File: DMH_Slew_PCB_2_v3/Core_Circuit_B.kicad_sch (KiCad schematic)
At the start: 48 parts, among them J6 TS_Jack_6.35mm_Sw, J60 Conn_01x08_PinHeader, J61 Conn_01x08_PinHeader, J7 TS_Jack_6.35mm_Sw, J8 TS_Jack_6.35mm_Sw, Q10 BC558, Q7 BC548, Q8 BC548, Q9 BC558, SW4 SW_DPDT_3way, SW5 SW_DPDT, SW6 SPDT_OnOffOn, U3 TL074, U4 TL074

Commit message: Relinked PCB1 and 2 with new v3 schematics
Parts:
- removed J60, J61: Conn_01x08_PinHeader, Connector_PinSocket_2.54mm:PinSocket_1x08_P2.54mm_Vertical, symbol SynthStuff:Conn_01x08_PinHeader
- removed R69, R70: 1k, Resistor_THT:R_Axial_DIN0207_L6.3mm_D2.5mm_P7.62mm_Horizontal, symbol Device:R_US
- removed R71, R72: 100k, Resistor_THT:R_Axial_DIN0207_L6.3mm_D2.5mm_P7.62mm_Horizontal, symbol Device:R_US
- removed R73: 220k, Resistor_THT:R_Axial_DIN0207_L6.3mm_D2.5mm_P7.62mm_Horizontal, symbol Device:R_US
- removed R74: 10k, Resistor_THT:R_Axial_DIN0207_L6.3mm_D2.5mm_P7.62mm_Horizontal, symbol Device:R_US
- removed R75, R76: 1k8, Resistor_THT:R_Axial_DIN0207_L6.3mm_D2.5mm_P7.62mm_Horizontal, symbol Device:R_US
- added C17: 10pF, Capacitor_THT:C_Disc_D3.0mm_W2.0mm_P2.50mm, symbol Device:C
- added C18: 220nF, Capacitor_THT:C_Disc_D4.3mm_W1.9mm_P5.00mm, symbol Device:C
- added C19: 22nF, Capacitor_THT:C_Disc_D4.3mm_W1.9mm_P5.00mm, symbol Device:C
- added C20: 2.2nF, Capacitor_THT:C_Disc_D4.3mm_W1.9mm_P5.00mm, symbol Device:C
- added J21, J23, J24, J26: Conn_02x03_Top_Bottom, Connector_PinHeader_2.54mm:PinHeader_2x03_P2.54mm_Horizontal, symbol Connector_Generic:Conn_02x03_Top_Bottom
- added J22, J25: Conn_02x06_Top_Bottom, Connector_PinHeader_2.54mm:PinHeader_2x06_P2.54mm_Horizontal, symbol Connector_Generic:Conn_02x06_Top_Bottom
- added J27, J28: Conn_01x08, Connector_PinHeader_2.54mm:PinHeader_1x08_P2.54mm_Vertical, symbol Connector_Generic:Conn_01x08
- added J29, J30: Conn_01x08, Connector_PinSocket_2.54mm:PinSocket_1x08_P2.54mm_Vertical, symbol Connector_Generic:Conn_01x08
- added R41: 56k, Resistor_THT:R_Axial_DIN0207_L6.3mm_D2.5mm_P7.62mm_Horizontal, symbol Device:R_US
- added R42, R43, R44, R56: 100k, Resistor_THT:R_Axial_DIN0207_L6.3mm_D2.5mm_P7.62mm_Horizontal, symbol Device:R_US
- added R55: 220k, Resistor_THT:R_Axial_DIN0207_L6.3mm_D2.5mm_P7.62mm_Horizontal, symbol Device:R_US
- added R61, R62: 1k, Resistor_THT:R_Axial_DIN0207_L6.3mm_D2.5mm_P7.62mm_Horizontal, symbol Device:R_US
- added unit 5 of U3
- added unit 5 of U4
- C22: value 220nF -> 10pF; footprint Capacitor_THT:C_Disc_D4.3mm_W1.9mm_P5.00mm -> Capacitor_THT:C_Disc_D3.0mm_W2.0mm_P2.50mm
- C23: value 22nF -> 100nF
- C24: value 2.2nF -> 100nF
- C25, C26: value 10pF -> 100nF; footprint Capacitor_THT:C_Disc_D3.0mm_W2.0mm_P2.50mm -> Capacitor_THT:C_Disc_D4.3mm_W1.9mm_P5.00mm
- Q7, Q9: footprint Package_TO_SOT_THT:TO-92L_Inline_Wide -> Package_TO_SOT_THT:TO-92_Inline
- R46: value 56k -> 100k
- R47: value 100k -> 1k
- R52: value 1k -> 100k
- R53: value 100k -> 56k
- R58: value 56k -> 220k
- R59, R60: value 100k -> 1k8
- R63: value 220k -> 100k
- R65: value 100k -> 220k
- R66: value 220k -> 10k
- U3: footprint Package_DIP:DIP-16_W7.62mm_Socket -> Package_DIP:DIP-14_W7.62mm_Socket
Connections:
- net +10V_B: now also R58.1, J21.2 (Pin_2), J24.2 (Pin_2), J27.5 (Pin_5), J29.5 (Pin_5), R55.1; no longer R63.1, R66.1
- net GND: now also C23.2, C24.1, C25.2, C26.1, R51.2, R52.2, R59.1, R60.2, R64.2, R65.2, J21.3 (Pin_3), J21.5 (Pin_5), J21.6 (Pin_6), J22.5 (Pin_5), J22.6 (Pin_6), J23.3 (Pin_3), J24.3 (Pin_3), J24.5 (Pin_5), J24.6 (Pin_6), J25.5 (Pin_5), J25.6 (Pin_6), J26.3 (Pin_3), J27.1 (Pin_1), J27.7 (Pin_7), J27.8 (Pin_8), J28.8 (Pin_8), J29.1 (Pin_1), J29.7 (Pin_7), J29.8 (Pin_8), J30.8 (Pin_8); no longer R57.2, R59.2
- net at Q10.1 (C), Q7.1 (C), U4.13 (-): now also C22.1, R63.1; no longer C26.1
- net at Q10.2 (B): now also R68.1
- net at Q10.3 (E), Q7.3 (E), Q8.3 (E)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: now also R66.1
- net at Q8.1 (C), Q9.1 (C), U4.6 (-): now also C18.1, C19.1, C20.1; no longer C22.1, C23.1, C24.1
- net at C22.2: now also R66.2, U4.14; no longer SW6.3 (C)
- net at U4.8: now also C21.2, R63.2, R65.1; no longer C25.2
- net at RV4.3, SW4.2 (B): now also R53.2; no longer R58.2
- net B_CV_Buff_C: now reaches SW4.3 (C), SW4.4 (A)
- net B_CV_Buff_C: now also J29.6 (Pin_6); no longer U3.1, U3.2 (-)
- net at RV3.3, SW4.5 (B): now also R41.2; no longer R46.2
- net B_CV_In_Jack_M: now reaches J7.T
- net B_CV_In_Jack_M: now also J26.5 (Pin_5); no longer R52.2
- net at U4.9 (-): now also C21.1, R62.1; no longer C25.1
- net B_Rng_Sw_p1_C: now reaches SW6.1 (A)
- net B_Rng_Sw_p1_C: now also J30.7 (Pin_7); no longer C23.2
- net -12V: now reaches C26.2
- net -12V: now also C24.2, J21.4 (Pin_4), J24.4 (Pin_4), U3.11 (V-), U4.11 (V-); no longer U4.14
- net at U4.7: now also R61.2
- net Comp_-R renamed B_Comp_-R
- net B_Comp_-R: now also R67.2, R44.1; no longer R53.1
- removed net Comp_F: Q9.2 (B), R47.1, R65.2, R66.2, R68.1
- removed net Comp_R: Q7.2 (B), R60.1, R63.2, R64.2, R67.2
- removed net Fall_CV: R46.1, R65.1, RV3.2
- net In B TN renamed B_Input_Jack_TN_M
- removed net Input: J6.T, R54.2, U4.10 (+)
- net Out B TN renamed B_Out_Jack_TN_M
- removed net Output: C24.2, J8.T, R51.2, SW6.2 (B)
- removed net Rise_CV: R58.1, R64.1, RV4.2
- new net: R47.1, R51.1, U3.3 (+)
- new net: R48.1, R52.1, U4.3 (+)
- new net: C17.1, R43.2, R46.1, U4.2 (-)
- new net +12V: C23.1, C25.1, J21.1 (Pin_1), J24.1 (Pin_1), U3.4 (V+), U4.4 (V+)
- new net B_CV_Buff_M: J25.4 (Pin_4), J27.6 (Pin_6)
- new net B_CV_Buff_S: J22.4 (Pin_4), U3.1, U3.2 (-)
- new net B_CV_In_Jack_S: J23.5 (Pin_5), R47.2
- new net B_Comp_F: Q9.2 (B), R42.1, R57.2, R58.2, R60.1
- new net B_Comp_R: Q7.2 (B), R54.1, R55.2, R56.2, R59.2
- new net B_Diff_Amp_C: J29.2 (Pin_2), SW5.1 (A)
- new net B_Diff_Amp_M: J25.1 (Pin_1), J27.2 (Pin_2)
- new net B_Diff_Amp_S: C17.2, J22.1 (Pin_1), R43.1, U4.1
- new net B_F_Gate_Jack_M: J26.1 (Pin_1)
- new net B_F_Gate_Jack_S: J23.1 (Pin_1)
- new net B_F_LED_C: J30.4 (Pin_4)
- new net B_F_LED_M: J25.10 (Pin_10), J28.4 (Pin_4)
- new net B_F_LED_S: J22.10 (Pin_10)
- new net B_Fall_CV_C: J29.4 (Pin_4), R41.1, RV3.2
- new net B_Fall_CV_M: J25.3 (Pin_3), J27.4 (Pin_4)
- new net B_Fall_CV_S: J22.3 (Pin_3), R57.1
- new net B_Input_Jack_M: J26.4 (Pin_4), J6.T
- new net B_Input_Jack_S: J23.4 (Pin_4), R48.2, R64.1, U4.10 (+)
- new net B_LinLog_Sw_p2_C: J30.2 (Pin_2), SW5.2 (B)
- new net B_LinLog_Sw_p2_M: J25.8 (Pin_8), J28.2 (Pin_2)
- new net B_LinLog_Sw_p2_S: J22.8 (Pin_8), R42.2, R44.2
- new net B_LinLog_Sw_p5_C: J30.1 (Pin_1), SW5.5 (B)
- new net B_LinLog_Sw_p5_M: J25.7 (Pin_7), J28.1 (Pin_1)
- new net B_LinLog_Sw_p5_S: J22.7 (Pin_7), R50.2, R54.2
- new net B_Out_Jack_C: J30.6 (Pin_6), SW6.2 (B)
- new net B_Out_Jack_M: J26.6 (Pin_6), J28.6 (Pin_6), J8.T
- new net B_Out_Jack_S: C20.2, J23.6 (Pin_6), R46.2, R61.1, R62.2
- new net B_R_Gate_Jack_M: J26.2 (Pin_2)
- new net B_R_Gate_Jack_S: J23.2 (Pin_2)
- new net B_R_LED_C: J30.3 (Pin_3)
- new net B_R_LED_M: J25.9 (Pin_9), J28.3 (Pin_3)
- new net B_R_LED_S: J22.9 (Pin_9)
- new net B_Rise_CV_C: J29.3 (Pin_3), R53.1, RV4.2
- new net B_Rise_CV_M: J25.2 (Pin_2), J27.3 (Pin_3)
- new net B_Rise_CV_S: J22.2 (Pin_2), R56.1
- new net B_Rng_Sw_p1_M: J25.12 (Pin_12), J28.7 (Pin_7)
- new net B_Rng_Sw_p1_S: C19.2, J22.12 (Pin_12)
- new net B_Rng_Sw_p3_C: J30.5 (Pin_5), SW6.3 (C)
- new net B_Rng_Sw_p3_M: J25.11 (Pin_11), J28.5 (Pin_5)
- new net B_Rng_Sw_p3_S: C18.2, J22.11 (Pin_11)
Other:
- note removed: "PCB 2"

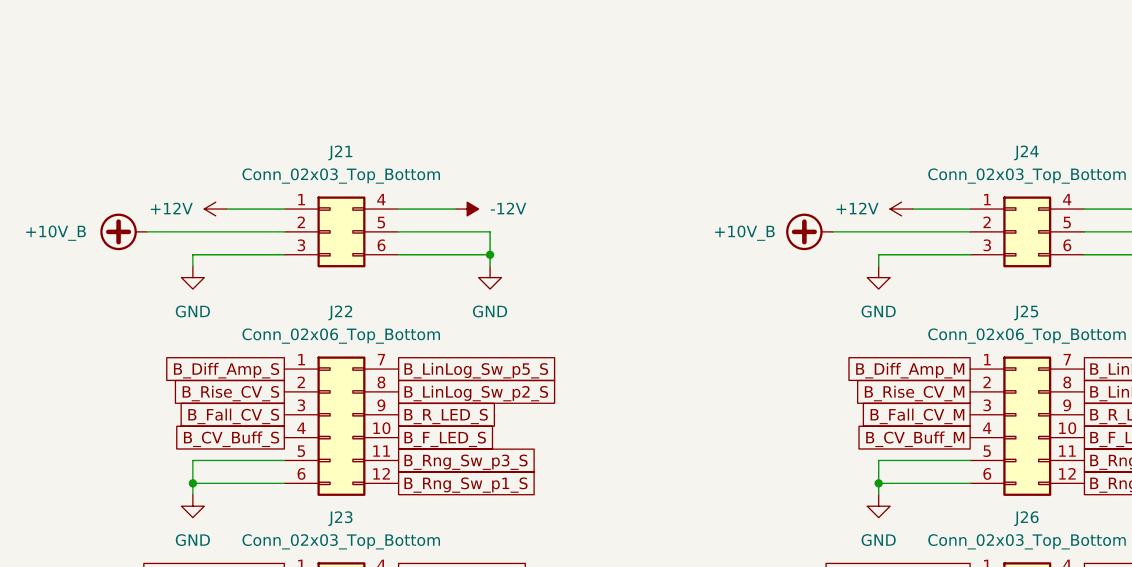
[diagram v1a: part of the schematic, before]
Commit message: PCB 1 routing in progress
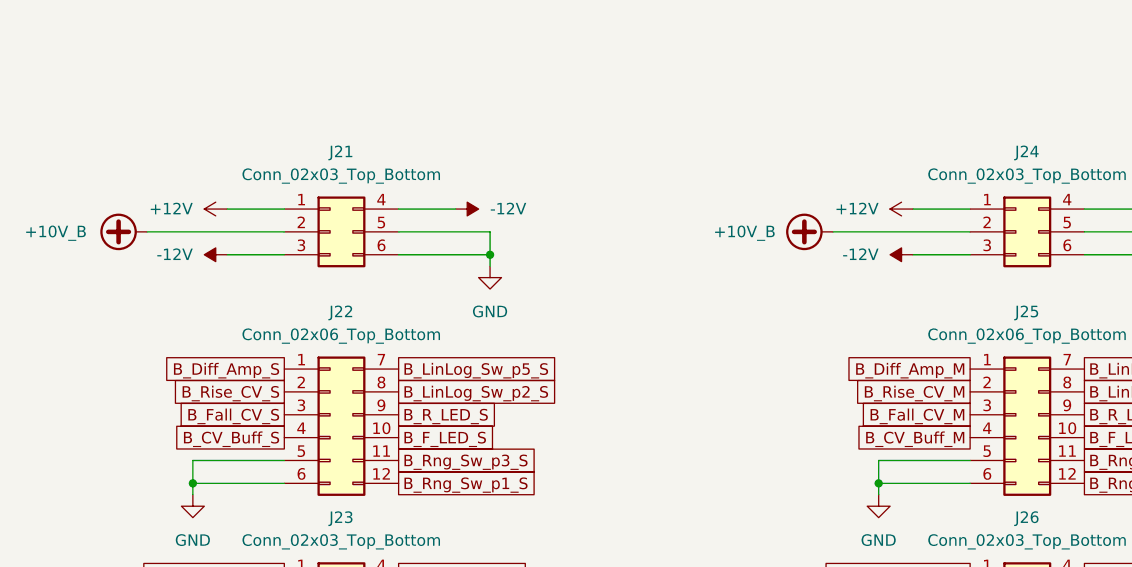
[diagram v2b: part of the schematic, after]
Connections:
- net -12V: now also J21.3 (Pin_3), J24.3 (Pin_3)
- net GND: no longer J21.3 (Pin_3), J24.3 (Pin_3)
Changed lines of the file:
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@@
 	(wire
 		(pts
-			(xy 34.29 231.14) (xy 44.45 231.14)
+			(xy 38.1 231.14) (xy 44.45 231.14)
 		)
 		(stroke
@@
 	(wire
 		(pts
-			(xy 34.29 232.41) (xy 34.29 231.14)
-		)
-		(stroke
-			(width 0)
-			(type default)
-		)
-	)
-	(wire
-		(pts
 			(xy 321.31 161.29) (xy 323.85 161.29)
 		)
@@
 	(wire
 		(pts
-			(xy 110.49 231.14) (xy 110.49 232.41)
-		)
-		(stroke
-			(width 0)
-			(type default)
-		)
-	)
-	(wire
-		(pts
 			(xy 264.16 135.89) (xy 266.7 135.89)
 		)
@@
 	(wire
 		(pts
-			(xy 120.65 231.14) (xy 110.49 231.14)
+			(xy 120.65 231.14) (xy 114.3 231.14)
 		)
 		(stroke
@@
 	)
 	(symbol
-		(lib_id "power:GND")
-		(at 34.29 232.41 0)
-		(mirror y)
-		(unit 1)
-		(exclude_from_sim no)
-		(in_bom yes)
-		(on_board no)
-		(dnp no)
-		(fields_autoplaced yes)
-		(property "Reference" "#PWR0106"
-			(at 34.29 238.76 0)
-			(effects
-				(font
-					(size 1.27 1.27)
-				)
-				(hide yes)
-			)
-		)
-		(property "Value" "GND"
-			(at 34.29 237.49 0)
-			(effects
-				(font
-					(size 1.27 1.27)
-				)
-			)
-		)
-		(property "Footprint" ""
-			(at 34.29 232.41 0)
-			(effects
-				(font
-					(size 1.27 1.27)
-				)
-				(hide yes)
-			)
-		)
-		(property "Datasheet" ""
-			(at 34.29 232.41 0)
-			(effects
-				(font
-					(size 1.27 1.27)
-				)
-				(hide yes)
-			)
-		)
-		(property "Description" "Power symbol creates a global label with name \"GND\" , ground"
-			(at 34.29 232.41 0)
-			(effects
-				(font
-					(size 1.27 1.27)
-				)
-				(hide yes)
-			)
-		)
-		(pin "1"
-		)
-		(instances
-			(project "DMH_Slew_PCB_2_v3"
-				(path "/58f4306d-5387-4983-bb08-41a2313fd315/77d402a4-d1d6-4e9c-af86-3ca5793147b8"
-					(reference "#PWR0106")
-					(unit 1)
-				)
-			)
-		)
-	)
-	(symbol
 		(lib_id "Transistor_BJT:BC558")
 		(at 228.6 173.99 270)
@@
 	)
 	(symbol
+		(lib_id "power:-12V")
+		(at 38.1 231.14 90)
+		(unit 1)
+		(exclude_from_sim no)
+		(in_bom yes)
+		(on_board no)
+		(dnp no)
+		(fields_autoplaced yes)
+		(property "Reference" "#PWR0106"
+			(at 41.91 231.14 0)
+			(effects
+				(font
+					(size 1.27 1.27)
+				)
+				(hide yes)
+			)
+		)
+		(property "Value" "-12V"
+			(at 34.29 231.1399 90)
+			(effects
+				(font
+					(size 1.27 1.27)
+				)
+				(justify left)
+			)
+		)
+		(property "Footprint" ""
+			(at 38.1 231.14 0)
+			(effects
+				(font
+					(size 1.27 1.27)
+				)
+				(hide yes)
+			)
+		)
+		(property "Datasheet" ""
+			(at 38.1 231.14 0)
+			(effects
+				(font
+					(size 1.27 1.27)
+				)
+				(hide yes)
+			)
+		)
+		(property "Description" "Power symbol creates a global label with name \"-12V\""
+			(at 38.1 231.14 0)
+			(effects
+				(font
+					(size 1.27 1.27)
+				)
+				(hide yes)
+			)
+		)
+		(pin "1"
+		)
+		(instances
+			(project "DMH_Slew_PCB_2_v3"
+				(path "/58f4306d-5387-4983-bb08-41a2313fd315/77d402a4-d1d6-4e9c-af86-3ca5793147b8"
+					(reference "#PWR0106")
+					(unit 1)
+				)
+			)
+		)
+	)
+	(symbol
 		(lib_id "power:GND")
 		(at 180.34 76.2 0)
@@
 	(symbol
 		(lib_id "power:GND")
-		(at 110.49 232.41 0)
-		(unit 1)
-		(exclude_from_sim no)
-		(in_bom yes)
-		(on_board no)
-		(dnp no)
-		(fields_autoplaced yes)
-		(property "Reference" "#PWR0113"
-			(at 110.49 238.76 0)
-			(effects
-				(font
-					(size 1.27 1.27)
-				)
-				(hide yes)
-			)
-		)
-		(property "Value" "GND"
-			(at 110.49 237.49 0)
-			(effects
-				(font
-					(size 1.27 1.27)
-				)
-			)
-		)
-		(property "Footprint" ""
-			(at 110.49 232.41 0)
-			(effects
-				(font
-					(size 1.27 1.27)
-				)
-				(hide yes)
-			)
-		)
-		(property "Datasheet" ""
-			(at 110.49 232.41 0)
-			(effects
-				(font
-					(size 1.27 1.27)
-				)
-				(hide yes)
-			)
-		)
-		(property "Description" "Power symbol creates a global label with name \"GND\" , ground"
-			(at 110.49 232.41 0)
-			(effects
-				(font
-					(size 1.27 1.27)
-				)
-				(hide yes)
-			)
-		)
-		(pin "1"
-		)
-		(instances
-			(project "DMH_Slew_PCB_2_v3"
-				(path "/58f4306d-5387-4983-bb08-41a2313fd315/77d402a4-d1d6-4e9c-af86-3ca5793147b8"
-					(reference "#PWR0113")
-					(unit 1)
-				)
-			)
-		)
-	)
-	(symbol
-		(lib_id "power:GND")
 		(at 82.55 97.79 0)
 		(unit 1)
@@
 					(unit 1)
 				)
+			)
+		)
+	)
+	(symbol
+		(lib_id "power:-12V")
+		(at 114.3 231.14 90)
+		(unit 1)
+		(exclude_from_sim no)
+		(in_bom yes)
+		(on_board no)
+		(dnp no)
+		(fields_autoplaced yes)
+		(property "Reference" "#PWR0113"
+			(at 118.11 231.14 0)
+			(effects
+				(font
+					(size 1.27 1.27)
+				)
+				(hide yes)
+			)
+		)
+		(property "Value" "-12V"
+			(at 110.49 231.1399 90)
+			(effects
+				(font
+					(size 1.27 1.27)
+				)
+				(justify left)
+			)
+		)
+		(property "Footprint" ""
+			(at 114.3 231.14 0)
+			(effects
+				(font
+					(size 1.27 1.27)
+				)
+				(hide yes)
+			)
+		)
+		(property "Datasheet" ""
+			(at 114.3 231.14 0)
+			(effects
+				(font
+					(size 1.27 1.27)
+				)
+				(hide yes)
+			)
+		)
+		(property "Description" "Power symbol creates a global label with name \"-12V\""
+			(at 114.3 231.14 0)
+			(effects
+				(font
+					(size 1.27 1.27)
+				)
+				(hide yes)
+			)
+		)
+		(pin "1"
+		)
+		(instances
+			(project "DMH_Slew_PCB_2_v3"
+				(path "/58f4306d-5387-4983-bb08-41a2313fd315/77d402a4-d1d6-4e9c-af86-3ca5793147b8"
+					(reference "#PWR0113")
+					(unit 1)
+				)

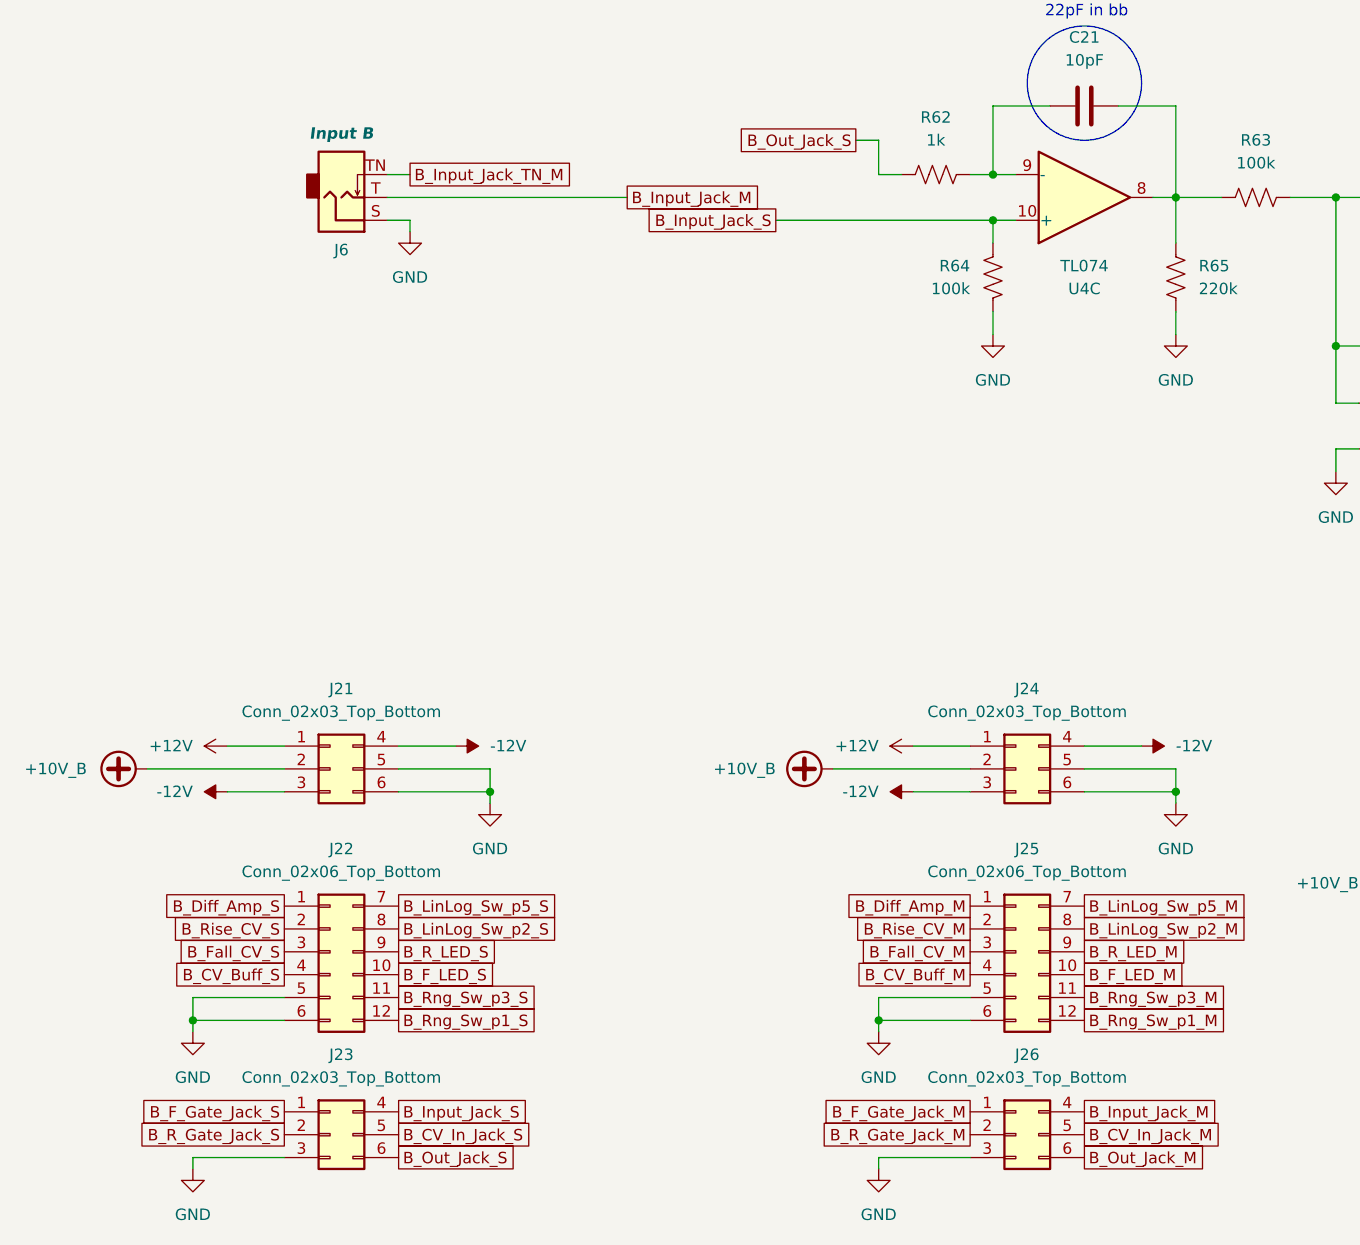
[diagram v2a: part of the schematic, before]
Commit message: Exposed loopback resistor to submodule connector
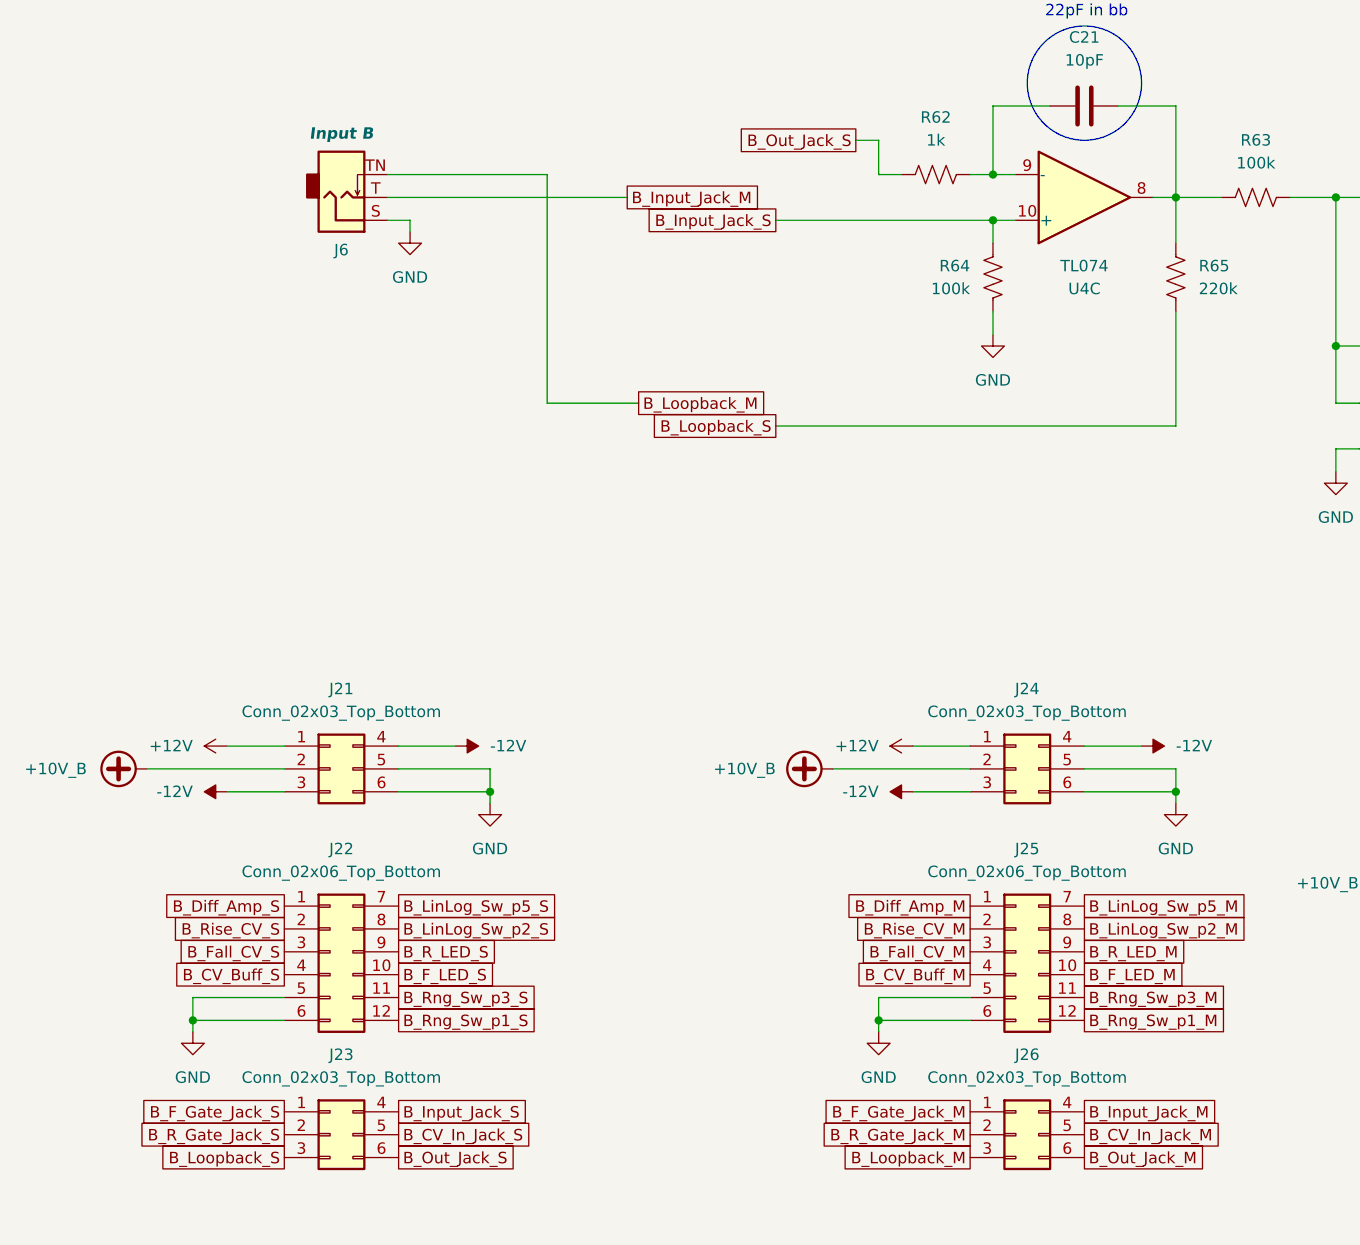
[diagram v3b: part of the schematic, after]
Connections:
- net GND: no longer J23.3 (Pin_3), J26.3 (Pin_3), R65.2
- net B_Input_Jack_TN_M renamed B_Loopback_M
- net B_Loopback_M: now also J26.3 (Pin_3)
- new net B_Loopback_S: J23.3 (Pin_3), R65.2
